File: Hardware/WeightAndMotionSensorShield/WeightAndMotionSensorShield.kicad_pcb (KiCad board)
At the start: 2 copper layers, 68.6 x 53.3 mm, 12 parts, among them J1 PIR, J2 CELLS, P1 Power, P2 Analog, P3 Digital, P4 Digital, P5 CONN_01X01, P6 CONN_01X01, P7 CONN_01X01, P8 CONN_01X01, U1 HX711_PCB

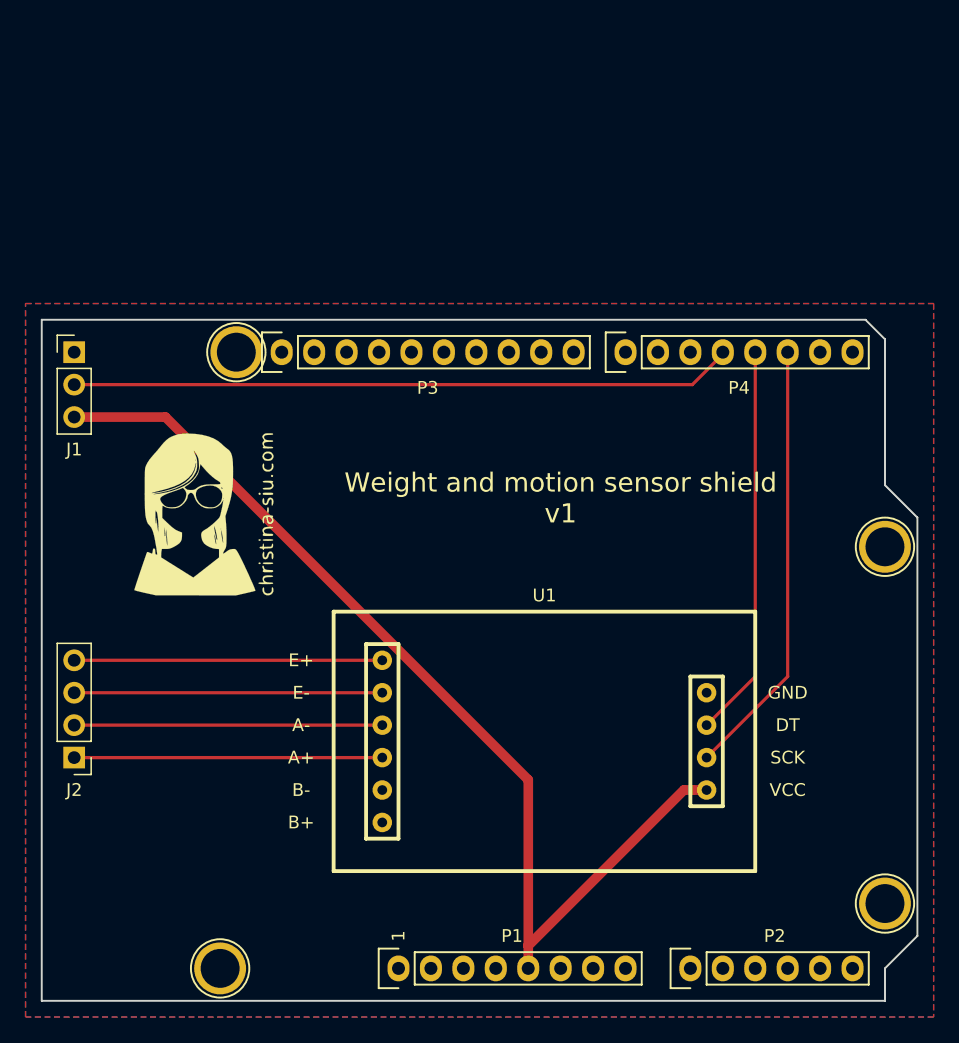
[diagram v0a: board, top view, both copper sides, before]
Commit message: Adds LED, reset button, 2nd PIR header
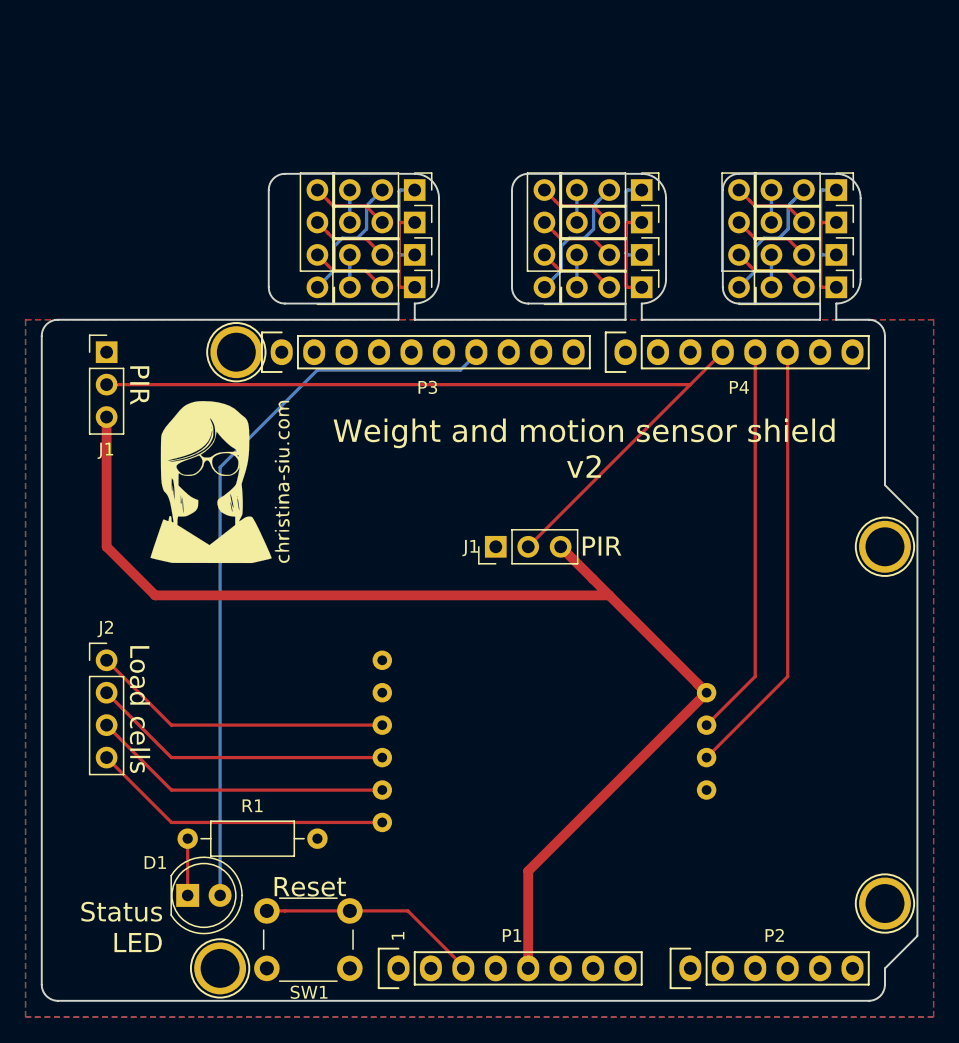
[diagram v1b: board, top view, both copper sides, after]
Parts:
- removed the G*** at (123.7, 88.3)
- removed the J1 at (113.5, 75.6)
- added D1: LED, LED_THT:LED_D5.0mm, F.Cu at (122.4, 118.1)
- added G***: Christina_Silk, WeightAndMotionSensor:Christina_Silk, B.Cu at (150.4, 106.0)
- added G***: Christina_Silk, WeightAndMotionSensor:Christina_Silk, F.Cu at (125.0, 85.7)
- added J1: PIR, Connector_PinHeader_2.54mm:PinHeader_1x03_P2.54mm_Vertical, F.Cu at (116.1, 75.6)
- added J1: PIR, Connector_PinHeader_2.54mm:PinHeader_1x03_P2.54mm_Vertical, F.Cu at (146.6, 90.8)
- added J3: UL, Connector_PinHeader_2.54mm:PinHeader_1x03_P2.54mm_Vertical, F.Cu at (140.2, 70.5)
- added J3: PIR, Connector_PinHeader_2.54mm:PinHeader_1x03_P2.54mm_Vertical, F.Cu at (158.0, 70.5)
- added J3: PIR, Connector_PinHeader_2.54mm:PinHeader_1x03_P2.54mm_Vertical, F.Cu at (173.2, 70.5)
- added J4: LL, Connector_PinHeader_2.54mm:PinHeader_1x03_P2.54mm_Vertical, F.Cu at (140.2, 65.4)
- added J4: PIR, Connector_PinHeader_2.54mm:PinHeader_1x03_P2.54mm_Vertical, F.Cu at (158.0, 65.4)
- added J4: PIR, Connector_PinHeader_2.54mm:PinHeader_1x03_P2.54mm_Vertical, F.Cu at (173.2, 65.4)
- added J5: CELLS, Connector_PinHeader_2.54mm:PinHeader_1x04_P2.54mm_Vertical, F.Cu at (132.6, 70.5)
- added J5: CELLS, Connector_PinHeader_2.54mm:PinHeader_1x04_P2.54mm_Vertical, F.Cu at (150.4, 70.5)
- added J5: CELLS, Connector_PinHeader_2.54mm:PinHeader_1x04_P2.54mm_Vertical, F.Cu at (165.6, 70.5)
- added J6: UR, Connector_PinHeader_2.54mm:PinHeader_1x03_P2.54mm_Vertical, F.Cu at (140.2, 67.9)
- added J6: PIR, Connector_PinHeader_2.54mm:PinHeader_1x03_P2.54mm_Vertical, F.Cu at (158.0, 67.9)
- added J6: PIR, Connector_PinHeader_2.54mm:PinHeader_1x03_P2.54mm_Vertical, F.Cu at (173.2, 67.9)
- added J7: LR, Connector_PinHeader_2.54mm:PinHeader_1x03_P2.54mm_Vertical, F.Cu at (140.2, 62.9)
- added J7: PIR, Connector_PinHeader_2.54mm:PinHeader_1x03_P2.54mm_Vertical, F.Cu at (158.0, 62.9)
- added J7: PIR, Connector_PinHeader_2.54mm:PinHeader_1x03_P2.54mm_Vertical, F.Cu at (173.2, 62.9)
- added R1: 128, Resistor_THT:R_Axial_DIN0207_L6.3mm_D2.5mm_P10.16mm_Horizontal, F.Cu at (132.6, 113.7)
- added SW1: RESET, Button_Switch_THT:SW_PUSH_6mm, F.Cu at (135.1, 123.8)
- U1: moved to B.Cu
- moved J2 8.03 mm to (116.1, 99.7), turned to 0 degrees
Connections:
- P1 pad 1: Net-(P1-Pad1) -> (no net)
- P1 pad 2: Net-(P1-Pad2) -> (no net)
- P1 pad 4: +3V3 -> (no net)
- P1 pad 8: Net-(P1-Pad8) -> (no net)
- P2 pad 1: Net-(P2-Pad1) -> (no net)
- P2 pad 2: Net-(P2-Pad2) -> (no net)
- P2 pad 3: Net-(P2-Pad3) -> (no net)
- P2 pad 4: Net-(P2-Pad4) -> (no net)
- P2 pad 5: Net-(P2-Pad5) -> (no net)
- P2 pad 6: Net-(P2-Pad6) -> (no net)
- P3 pad 1: Net-(P3-Pad1) -> (no net)
- P3 pad 10: Net-(P3-Pad10) -> (no net)
- P3 pad 2: Net-(P3-Pad2) -> (no net)
- P3 pad 3: Net-(P3-Pad3) -> (no net)
- P3 pad 5: Net-(P3-Pad5) -> (no net)
- P3 pad 6: Net-(P3-Pad6) -> (no net)
- P3 pad 8: Net-(P3-Pad8) -> (no net)
- P3 pad 9: Net-(P3-Pad9) -> (no net)
- P4 pad 1: Net-(P4-Pad1) -> (no net)
- P4 pad 2: Net-(P4-Pad2) -> (no net)
- P4 pad 3: Net-(P4-Pad3) -> (no net)
- P4 pad 7: Net-(P4-Pad7) -> (no net)
- P4 pad 8: Net-(P4-Pad8) -> (no net)
- P5 pad 1: Net-(P5-Pad1) -> (no net)
- P6 pad 1: Net-(P6-Pad1) -> (no net)
- P7 pad 1: Net-(P7-Pad1) -> (no net)
- P8 pad 1: Net-(P8-Pad1) -> (no net)
- U1 pad 5: Net-(U1-Pad5) -> (no net)
- U1 pad 6: Net-(U1-Pad6) -> (no net)
- U1 pad 8: /3(**) -> /2
- U1 pad 9: /2 -> /3(**)
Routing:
- net Net-(D1-Pad2): track 0.00 -> 57.4 mm
- net Net-(J5-Pad1): track 0.00 -> 31.2 mm
- net Net-(J3-Pad1): track 0.00 -> 22.2 mm
- net Net-(J6-Pad1): track 0.00 -> 22.2 mm
- net Net-(J3-Pad2): track 0.00 -> 18.4 mm
- net Net-(J4-Pad2): track 0.00 -> 18.4 mm
- net Net-(J5-Pad3): track 0.00 -> 18.4 mm
- net Net-(P1-Pad3): track 0.00 -> 17.3 mm
- net /4: track 51.9 -> 67.4 mm
- net +5V: track 81.1 -> 95.7 mm
- net Net-(J3-Pad3): track 0.00 -> 7.62 mm
- net Net-(J4-Pad3): track 0.00 -> 7.62 mm
- net Net-(D1-Pad1): track 0.00 -> 4.44 mm
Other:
- board size 68.6 x 53.3 mm -> 68.6 x 64.8 mm
- board text added: "Load cells"
- board text added: "PIR"
- board text added: "Reset"
- board text added: "Save the planet GO VEGAN"
- board text added: "Status LED"
- board text added: "Weight and motion sensor shield v2"
- board text removed: "Weight and motion sensor shield v1"

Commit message: PCB v1.1 and 2 changes
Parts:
- added J3: UL, Connector_PinHeader_2.54mm:PinHeader_1x03_P2.54mm_Vertical, F.Cu at (123.0, 57.5)
- added J3: UL, Connector_PinHeader_2.54mm:PinHeader_1x03_P2.54mm_Vertical, F.Cu at (122.9, 69.0)
- added J4: LL, Connector_PinHeader_2.54mm:PinHeader_1x03_P2.54mm_Vertical, F.Cu at (123.0, 54.5)
- added J4: LL, Connector_PinHeader_2.54mm:PinHeader_1x03_P2.54mm_Vertical, F.Cu at (122.9, 65.9)
- added J5: CELLS, Connector_PinHeader_2.54mm:PinHeader_1x04_P2.54mm_Vertical, F.Cu at (115.1, 59.0)
- added J5: CELLS, Connector_PinHeader_2.54mm:PinHeader_1x04_P2.54mm_Vertical, F.Cu at (115.1, 70.4)
- added J6: UR, Connector_PinHeader_2.54mm:PinHeader_1x03_P2.54mm_Vertical, F.Cu at (123.0, 56.0)
- added J6: UR, Connector_PinHeader_2.54mm:PinHeader_1x03_P2.54mm_Vertical, F.Cu at (122.9, 67.4)
- added J7: LR, Connector_PinHeader_2.54mm:PinHeader_1x03_P2.54mm_Vertical, F.Cu at (123.0, 53.0)
- added J7: LR, Connector_PinHeader_2.54mm:PinHeader_1x03_P2.54mm_Vertical, F.Cu at (122.9, 64.4)
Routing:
- net Net-(J5-Pad1): track 31.2 -> 50.4 mm
- net Net-(J4-Pad2): track 18.4 -> 32.0 mm
- net Net-(J5-Pad3): track 18.4 -> 30.8 mm
- net Net-(J3-Pad2): track 18.4 -> 30.0 mm
- net Net-(J3-Pad1): track 22.2 -> 31.4 mm
- net Net-(J6-Pad1): track 22.2 -> 31.4 mm
- net Net-(J3-Pad3): track 7.62 -> 10.7 mm
- net Net-(J4-Pad3): track 7.62 -> 10.7 mm
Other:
- board size 68.6 x 64.8 mm -> 68.6 x 76.3 mm

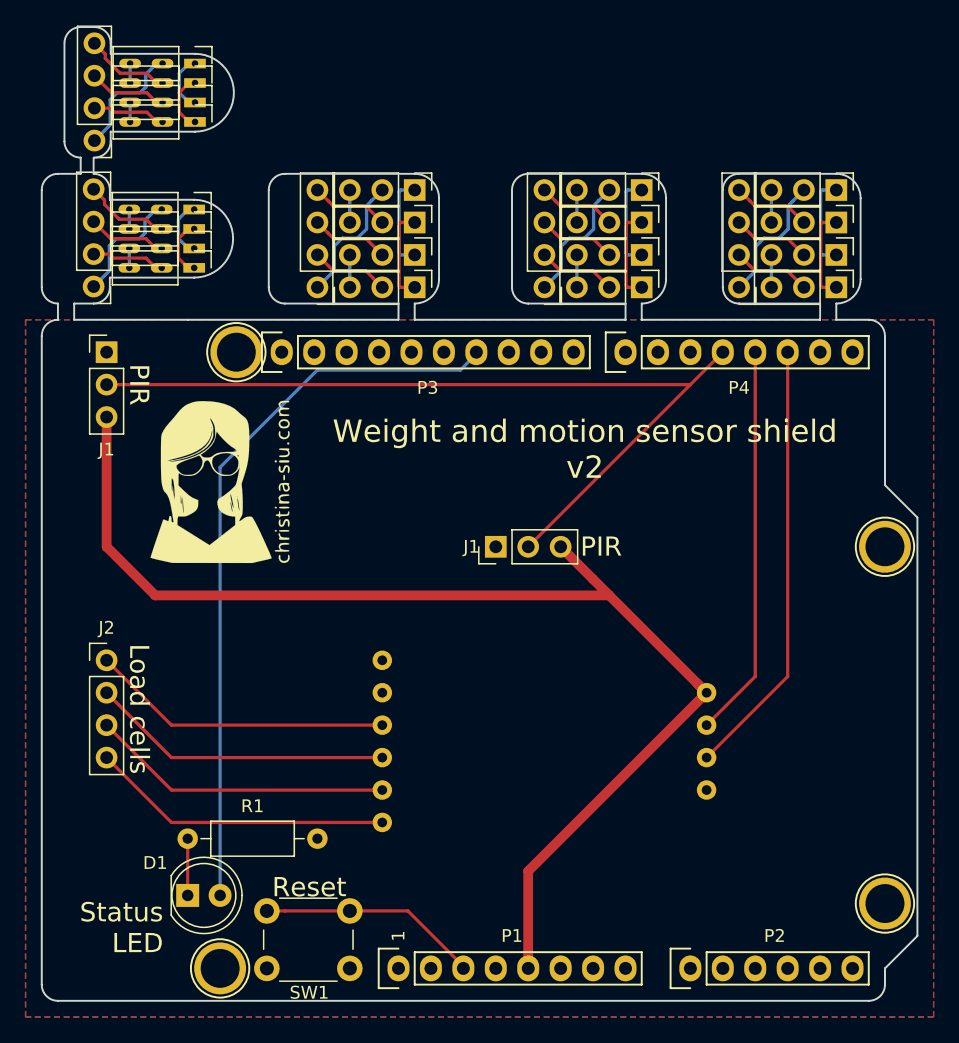
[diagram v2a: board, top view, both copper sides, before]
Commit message: Add header for HC-05 module
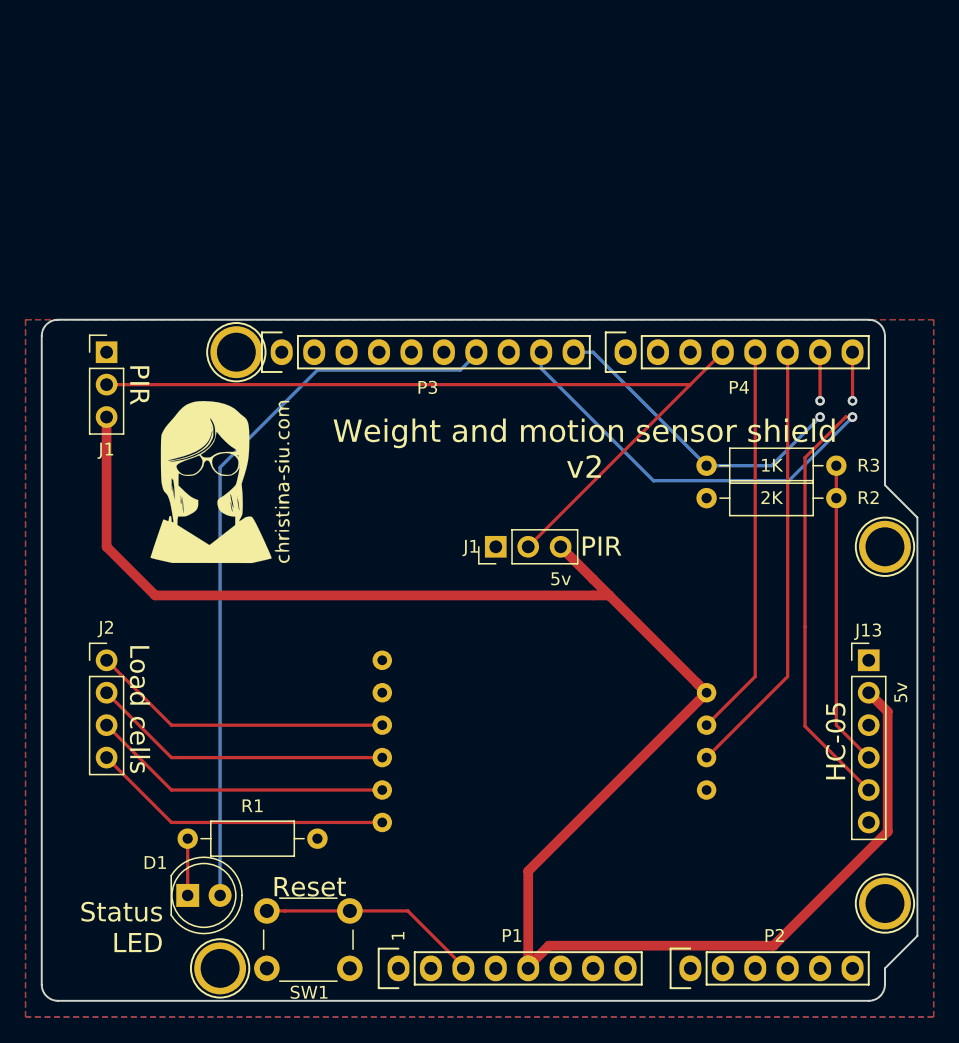
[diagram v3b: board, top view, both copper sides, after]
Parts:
- removed J3 (x3): UL, Connector_PinHeader_2.54mm:PinHeader_1x03_P2.54mm_Vertical
- removed J3 (x2), J4 (x2), J6 (x2), J7 (x2): PIR, Connector_PinHeader_2.54mm:PinHeader_1x03_P2.54mm_Vertical
- removed J4 (x3): LL, Connector_PinHeader_2.54mm:PinHeader_1x03_P2.54mm_Vertical
- removed J5 (x5): CELLS, Connector_PinHeader_2.54mm:PinHeader_1x04_P2.54mm_Vertical
- removed J6 (x3): UR, Connector_PinHeader_2.54mm:PinHeader_1x03_P2.54mm_Vertical
- removed J7 (x3): LR, Connector_PinHeader_2.54mm:PinHeader_1x03_P2.54mm_Vertical
- added J13: BT, Connector_PinHeader_2.54mm:PinHeader_1x06_P2.54mm_Vertical, F.Cu at (175.8, 99.7)
- added R2: 2K, Resistor_THT:R_Axial_DIN0207_L6.3mm_D2.5mm_P10.16mm_Horizontal, F.Cu at (163.1, 87.0)
- added R3: 1K, Resistor_THT:R_Axial_DIN0207_L6.3mm_D2.5mm_P10.16mm_Horizontal, F.Cu at (163.1, 84.5)
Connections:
- P1 pad 1: (no net) -> Net-(P1-Pad1)
- P1 pad 2: (no net) -> Net-(P1-Pad2)
- P1 pad 4: (no net) -> +3V3
- P1 pad 8: (no net) -> Net-(P1-Pad8)
- P2 pad 1: (no net) -> Net-(P2-Pad1)
- P2 pad 2: (no net) -> Net-(P2-Pad2)
- P2 pad 3: (no net) -> Net-(P2-Pad3)
- P2 pad 4: (no net) -> Net-(P2-Pad4)
- P2 pad 5: (no net) -> Net-(P2-Pad5)
- P2 pad 6: (no net) -> Net-(P2-Pad6)
- P3 pad 1: (no net) -> Net-(P3-Pad1)
- P3 pad 10: (no net) -> Net-(P3-Pad10)
- P3 pad 2: (no net) -> Net-(P3-Pad2)
- P3 pad 3: (no net) -> Net-(P3-Pad3)
- P3 pad 5: (no net) -> Net-(P3-Pad5)
- P3 pad 6: (no net) -> Net-(P3-Pad6)
- P3 pad 8: (no net) -> Net-(P3-Pad8)
- P3 pad 9: (no net) -> /9(**)
- P4 pad 1: (no net) -> Net-(P4-Pad1)
- P4 pad 2: (no net) -> Net-(P4-Pad2)
- P4 pad 3: (no net) -> Net-(P4-Pad3)
- P4 pad 7: (no net) -> Net-(P4-Pad7)
- P4 pad 8: (no net) -> Net-(P4-Pad8)
- P5 pad 1: (no net) -> Net-(P5-Pad1)
- P6 pad 1: (no net) -> Net-(P6-Pad1)
- P7 pad 1: (no net) -> Net-(P7-Pad1)
- P8 pad 1: (no net) -> Net-(P8-Pad1)
- U1 pad 5: (no net) -> Net-(U1-Pad5)
- U1 pad 6: (no net) -> Net-(U1-Pad6)
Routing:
- net /9(**): track 0.00 -> 65.3 mm, vias 0 -> 1
- net Net-(J5-Pad1): track 50.4 -> 0.00 mm
- net +5V: track 95.7 -> 139.9 mm
- net Net-(J4-Pad2): track 32.0 -> 0.00 mm
- net Net-(J3-Pad1): track 31.4 -> 0.00 mm
- net Net-(J6-Pad1): track 31.4 -> 0.00 mm
- net Net-(J5-Pad3): track 30.8 -> 0.00 mm
- net Net-(J3-Pad2): track 30.0 -> 0.00 mm
- net Net-(P3-Pad10): track 0.00 -> 24.6 mm, vias 0 -> 1
- net Net-(J13-Pad4): track 0.00 -> 23.9 mm
- net Net-(J3-Pad3): track 10.7 -> 0.00 mm
- net Net-(J4-Pad3): track 10.7 -> 0.00 mm
- net Net-(P4-Pad7): track 0.00 -> 3.96 mm, vias 0 -> 1
- net Net-(P4-Pad8): track 0.00 -> 3.81 mm, vias 0 -> 1
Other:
- board size 68.6 x 76.3 mm -> 68.6 x 53.3 mm
- board text added: "1K"
- board text added: "2K"
- board text added: "5v"
- board text added: "HC-05"
